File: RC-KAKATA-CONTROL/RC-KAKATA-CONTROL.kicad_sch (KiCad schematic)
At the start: 67 parts, among them J1 Conn_02x20_Socket_DG250T-5.0-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, J10 DB125-2.54-4P-GN, J12 Conn_01x07, J25 Conn_02x20_Socket_DG250T-5.0-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, J6 Raspberry_Pi_2x20_PTH, J8 DB125-2.54-4P-GN, U3 STM32H743IIT6, U8 W25Q128JVSIQTR, X1 SMD3225-4, X2 Q13MC3061000300

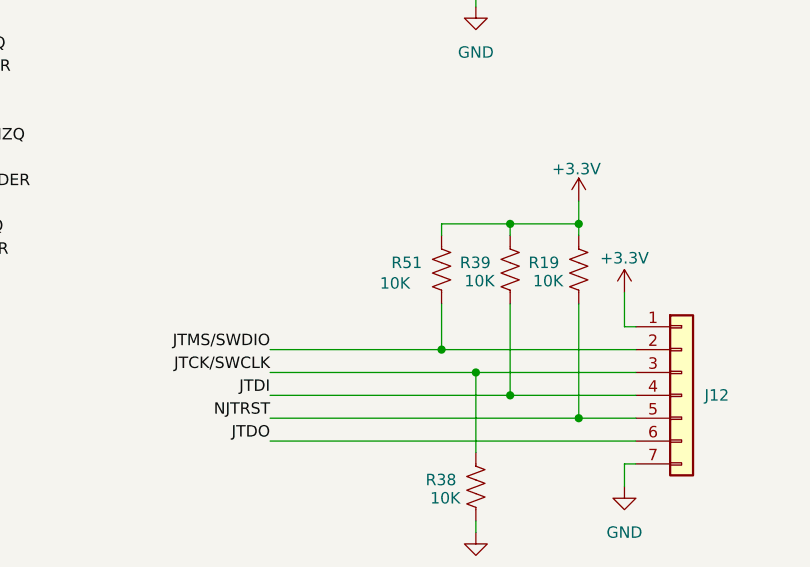
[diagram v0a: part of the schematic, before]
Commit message: Asignacion Ref. LCSC BOM
Asignacion de número de piezas de LCSC.
Queda pendiente por asignación:
-Cristal 25MHz
-Power Supply

Queda pendiente por realización:
-Acomodar las referencias para que no se solapen.
Att.: Juan y Eric
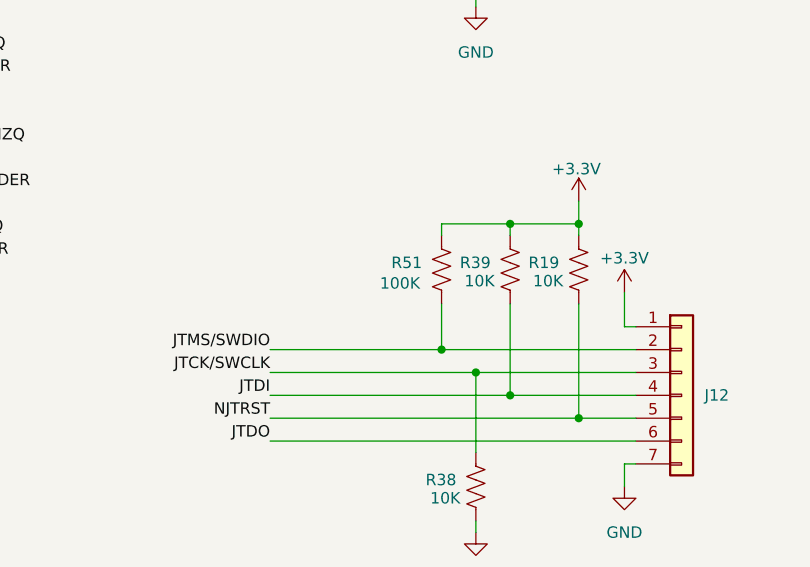
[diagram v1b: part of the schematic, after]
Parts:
- R51: value 10K -> 100K; LCSC Part C95204 -> C14675
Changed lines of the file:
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@@
 			)
 		)
-		(property "Value" "10K"
+		(property "Value" "100K"
 			(at 316.992 99.314 0)
 			(effects
@@
 			)
 		)
-		(property "LCSC Part" "C95204"
+		(property "LCSC Part" "C14675"
 			(at 323.85 97.79 0)
 			(effects
